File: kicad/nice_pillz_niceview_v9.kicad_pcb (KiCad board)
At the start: 2 copper layers, 100 x 86 mm, 28 parts, among them J1 Conn_01x13, J2 Conn_01x13, J3 Conn_01x13, J4 Conn_01x13, J5 Conn_01x10, J6 Conn_01x10, J7 Conn_01x13, J8 Conn_01x13, J9 NiceView, M1 MountingHole_6.4mm_M6, M3 MountingHole_4.3mm_M4, M4 MountingHole_4.3mm_M4, U1 nice!nanov2, U2 74HC595

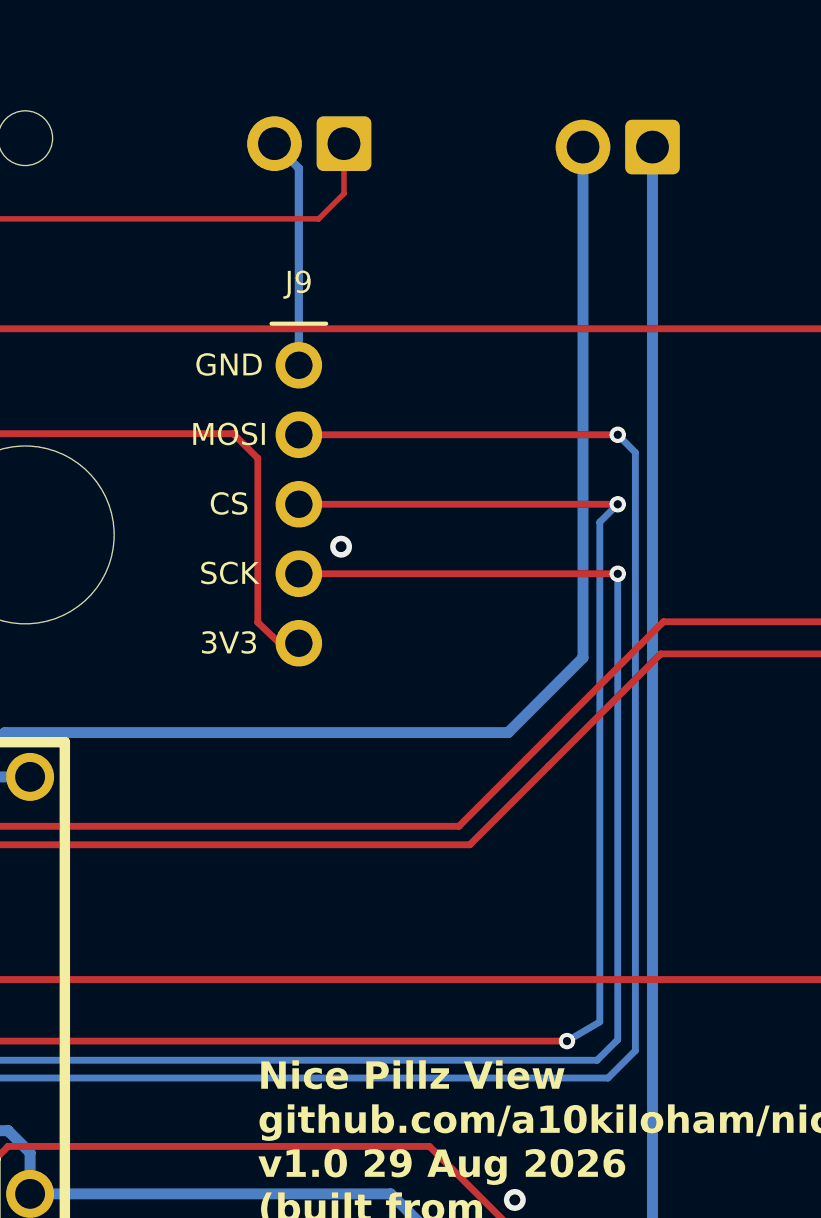
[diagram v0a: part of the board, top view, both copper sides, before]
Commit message: PCB: reorder J9 display header to match nice!view pinout
J9 now reads CS, GND, 3V3, SCK, MOSI top to bottom. Pad numbers and
nets are unchanged (schematic parity kept); pad positions and silk
labels moved within the footprint instance and the five connections
were rerouted. DRC (KiCad 10, zones refilled): no new violations,
0 unconnected items.

Co-Authored-By: Claude Fable 5.1 <noreply@anthropic.com>
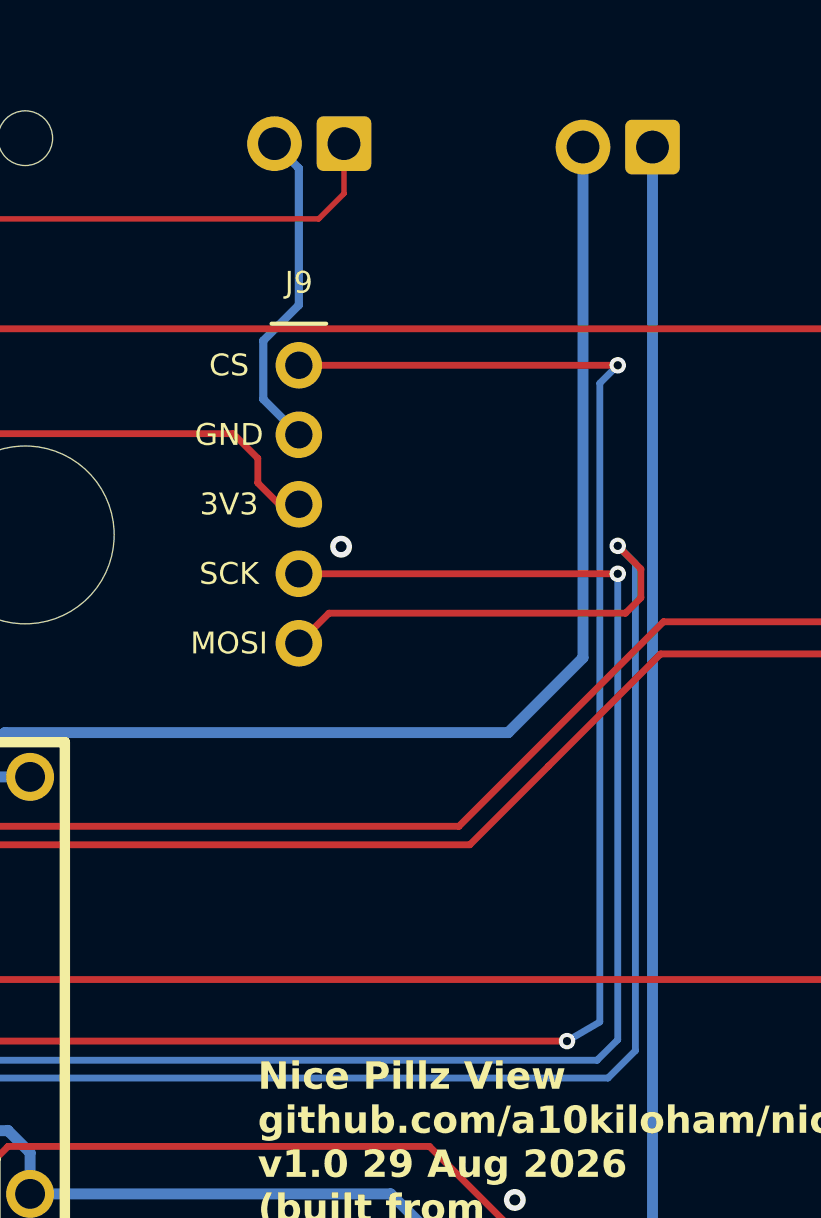
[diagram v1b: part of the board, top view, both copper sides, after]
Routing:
- net +5V: track 60.1 -> 55.0 mm
- net /LED_CAPS_LOCK: track 85.1 -> 90.1 mm
- net GND: track 63.3 -> 66.9 mm

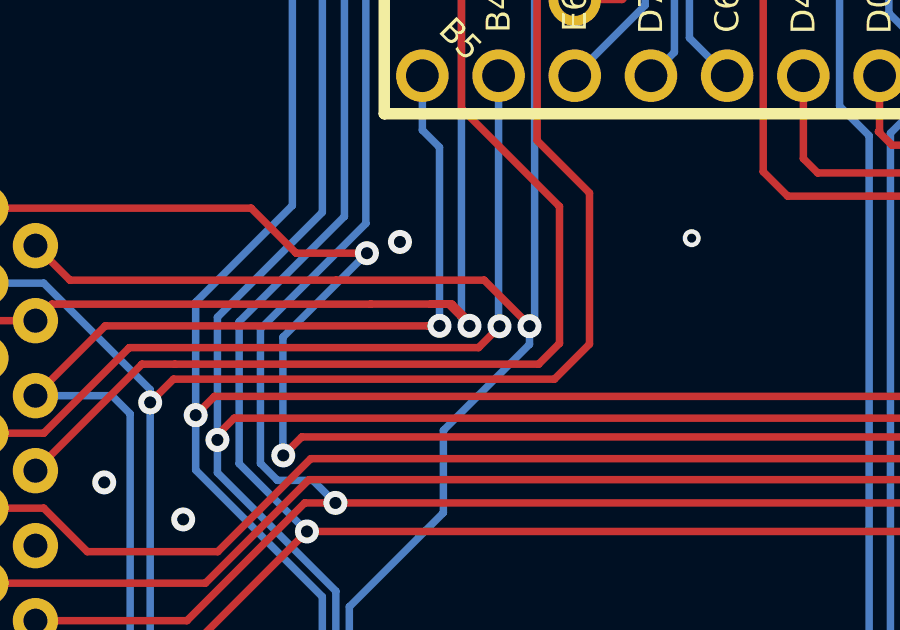
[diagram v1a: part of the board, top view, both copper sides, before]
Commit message: Repo cleanup and JLCPCB fabrication files
- kicad/jlcpcb: Gerbers (Protel ext, mask-subtracted silk), Excellon
  PTH/NPTH drills with maps, and a ready-to-upload zip, generated with
  kicad-cli from the committed board.
- PCB: remove a dangling ROW_3 track stub (DRC now 74 pre-existing
  warnings/errors, 0 unconnected).
- Drop stray .DS_Store files, the empty .gitkeep and the per-user
  .kicad_prl; extend .gitignore accordingly.
- README: ordering / regeneration instructions.

Co-Authored-By: Claude Fable 5.1 <noreply@anthropic.com>
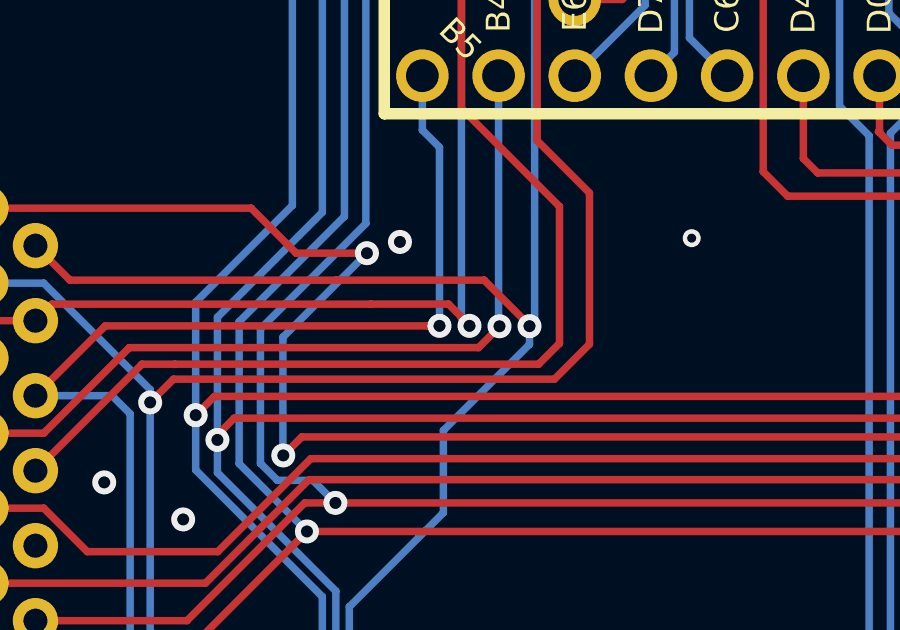
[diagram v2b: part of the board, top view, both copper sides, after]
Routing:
- net /ROW_3: track 75.4 -> 73.7 mm
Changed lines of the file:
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@@
-	)
-	(segment
-		(start 121.269003 106.780563)
-		(end 121.269003 106.92356)
-		(width 0.25)
-		(layer "F.Cu")
-		(net "/ROW_3")
-	)
-	(segment
-		(start 119.968695 106.19856)
-		(end 120.687 106.19856)
-		(width 0.25)
-		(layer "F.Cu")
-		(net "/ROW_3")
 	)
 	(segment
@@
 		(width 0.25)
 		(layer "F.Cu")
-		(net "/ROW_3")
-	)
-	(segment
-		(start 120.687 106.19856)
-		(end 121.269003 106.780563)
-		(width 0.25)
-		(layer "F.Cu")
